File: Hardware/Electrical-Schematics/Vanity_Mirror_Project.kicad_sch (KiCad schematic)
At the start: 38 parts, among them J1 USB_C_Receptacle_USB2.0_14P, SW1 RST, U1 CH340C, U2 ESP-12F, U3 USBLC6-2SC6, U4 XL1509-3.3, U5 SN74AHCT125N, U6 MPR121QR2

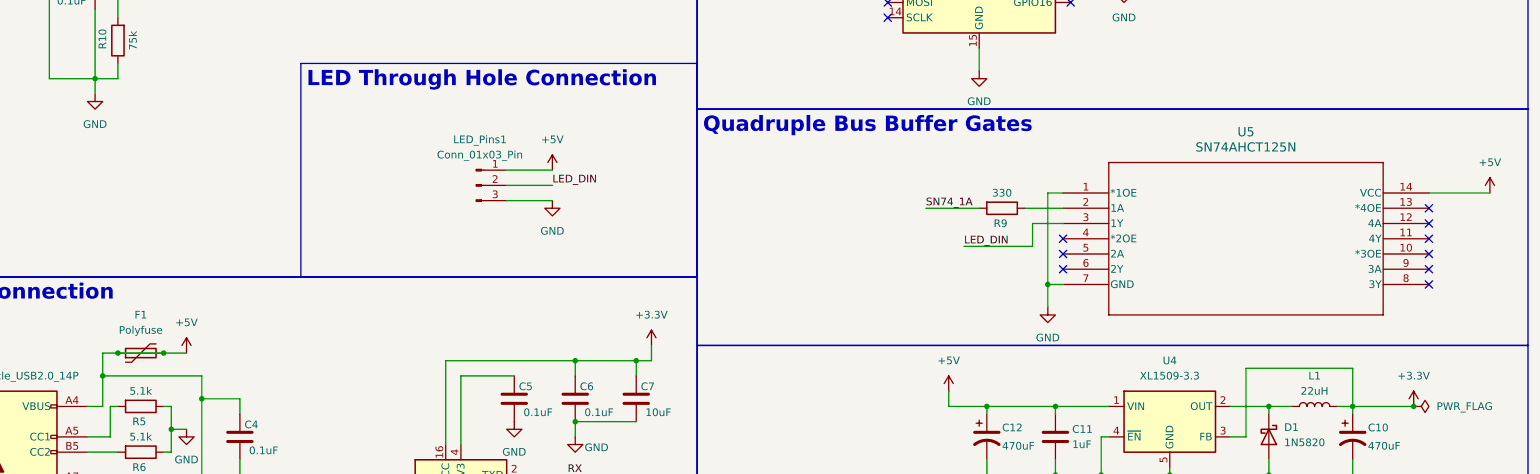
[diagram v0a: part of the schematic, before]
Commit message: PCB Design Progress
Made progress with the PCB design and reorganized the gitignores so that it works.
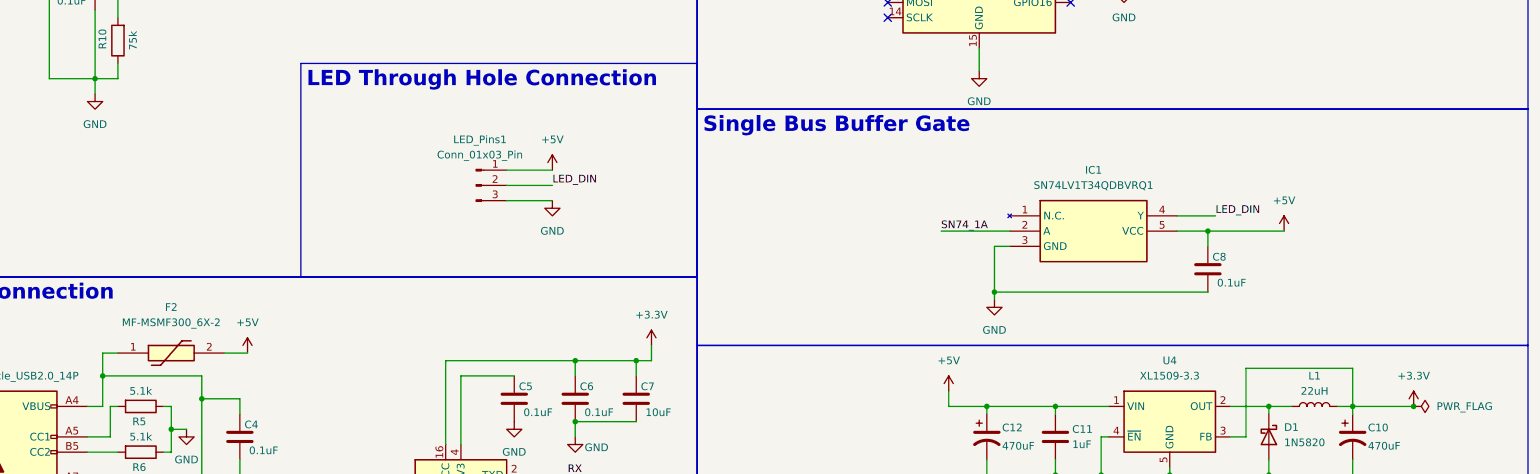
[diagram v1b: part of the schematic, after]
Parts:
- removed F1: Polyfuse, Fuse:Fuse_1206_3216Metric, symbol Device:Polyfuse
- removed R9: 330, Resistor_SMD:R_0603_1608Metric, symbol Device:R
- removed U5: SN74AHCT125N, VanityMirror_FootPrints:SN74AHCT125N, symbol New_Library:SN74AHCT125N
- added C8: 0.1uF, Capacitor_SMD:C_0603_1608Metric, symbol Device:C
- added F2: MF-MSMF300_6X-2, VanityMirror_FootPrints:MFMSMF3006X2, symbol New_Library:MF-MSMF300_6X-2
- added IC1: SN74LV1T34QDBVRQ1, VanityMirror_FootPrints:SOT95P280X145-5N, symbol New_Library:SN74LV1T34QDBVRQ1
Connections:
- net +5V: now also C8.1, F2.2, IC1.5 (VCC); no longer C4.1, J1.A4 (VBUS), J1.A9 (VBUS), J1.B4 (VBUS), J1.B9 (VBUS), U3.5 (VBUS)
- net GND: now also C8.2, IC1.3 (GND)
- net LED_DIN: now also IC1.4 (Y)
- net SN74_1A: now also IC1.2 (A)
- new net: C4.1, F2.1, J1.A4 (VBUS), J1.A9 (VBUS), J1.B4 (VBUS), J1.B9 (VBUS), U3.5 (VBUS)
- no-connect marks 32 -> 23

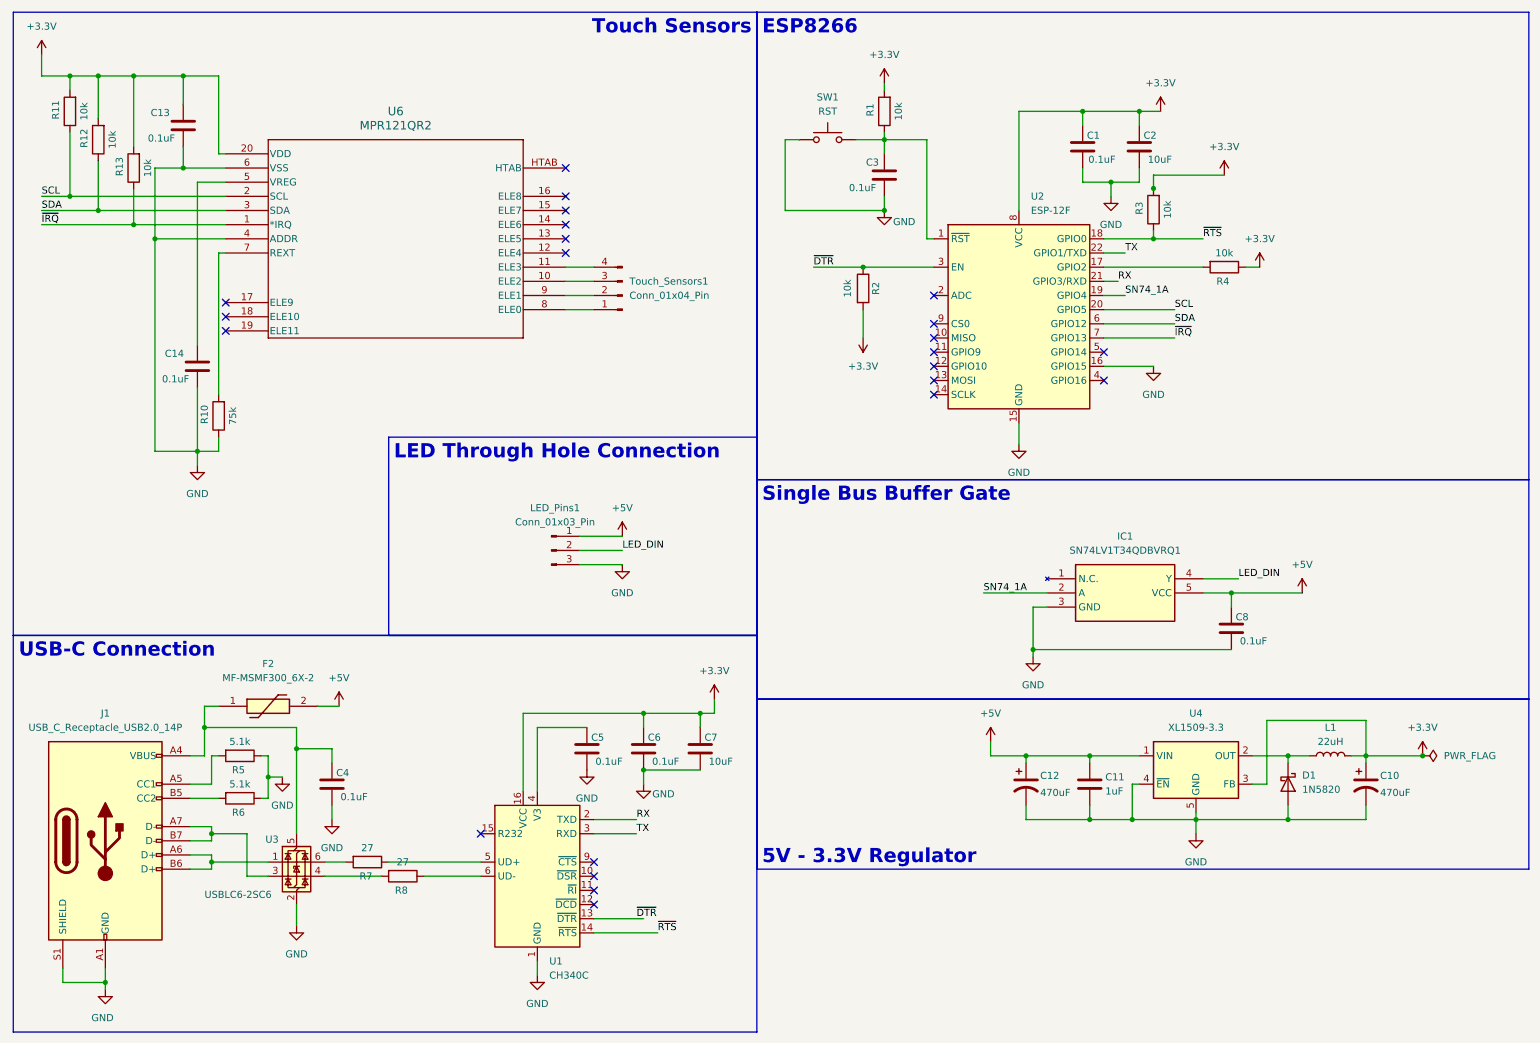
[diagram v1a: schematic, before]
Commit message: Initial PCB layout and Schematic Revisions
Revised some wiring in the schematic and fixed some wiring mistakes. Created an initial layout for the PCB
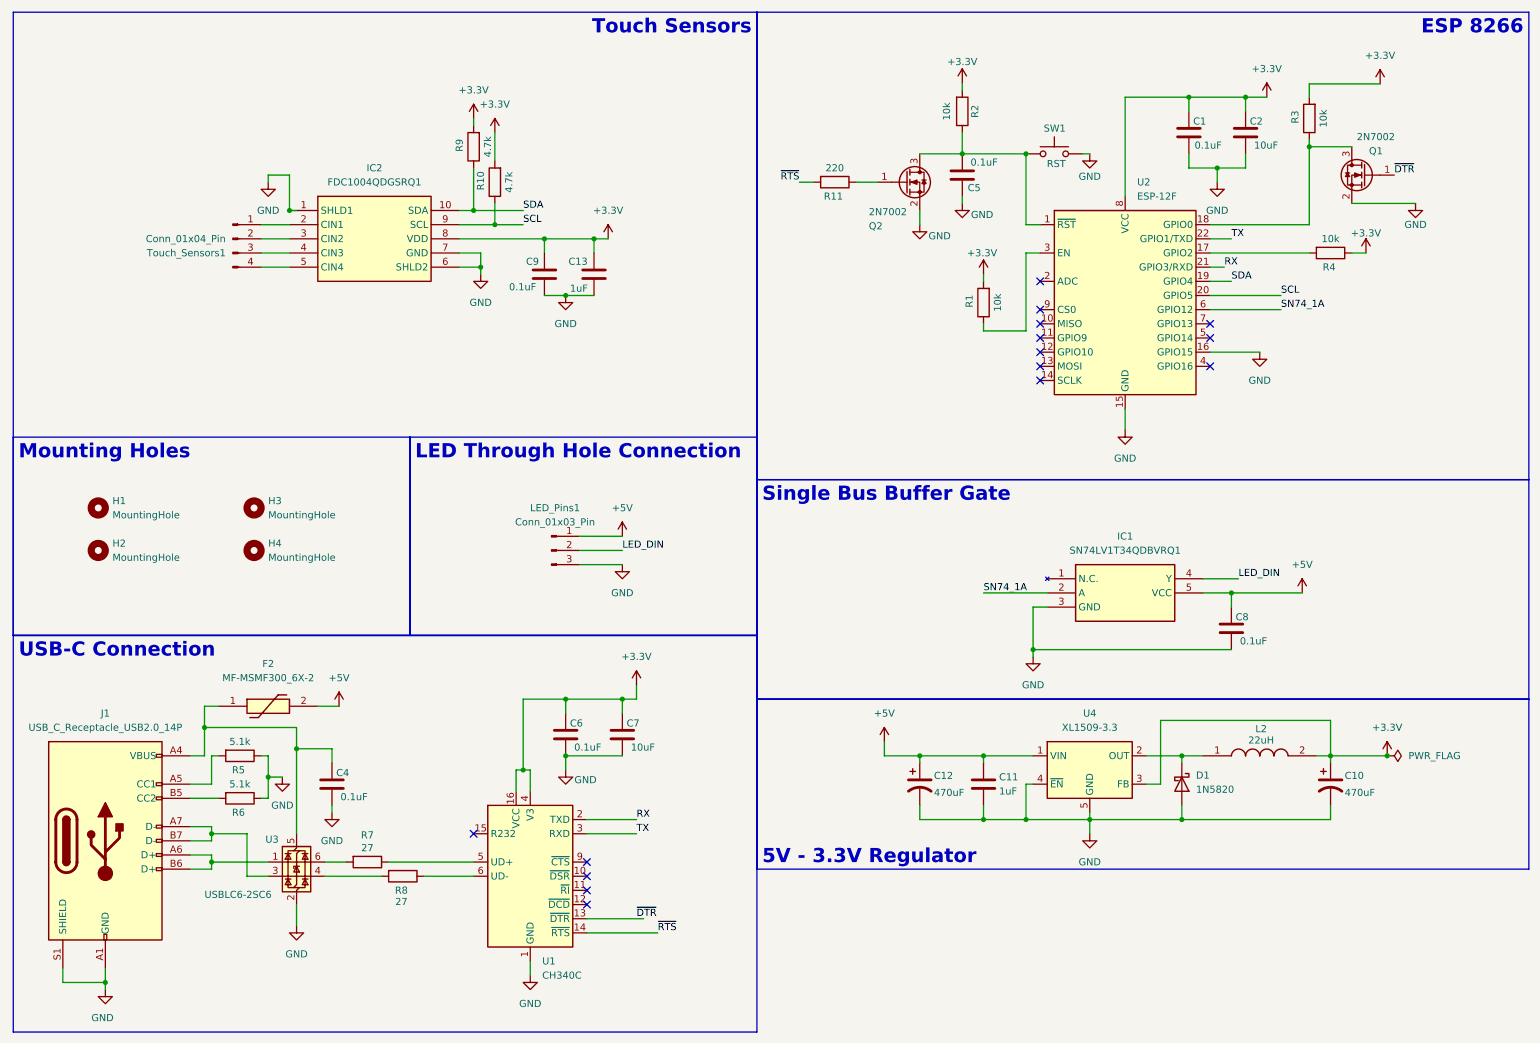
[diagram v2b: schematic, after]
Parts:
- removed C14, C3: 0.1uF, Capacitor_SMD:C_0603_1608Metric, symbol Device:C
- removed L1: 22uH, Inductor_SMD:L_Bourns_SRP1038C_10.0x10.0mm, symbol Device:L
- removed R12, R13: 10k, Resistor_SMD:R_0603_1608Metric, symbol Device:R
- removed U6: MPR121QR2, VanityMirror_FootPrints:QFN20_FRE, symbol New_Library:MPR121QR2
- added C9: 0.1uF, Capacitor_SMD:C_0603_1608Metric, symbol Device:C
- added H1, H2, H3, H4: MountingHole, MountingHole:MountingHole_3.2mm_M3, symbol Mechanical:MountingHole
- added IC2: FDC1004QDGSRQ1, SOP50P490X110-10N, symbol New_Library:FDC1004QDGSRQ1
- added L2: 22uH, INDPM110100X400N, symbol New_Library:SRP1038CC-220M
- added Q1, Q2: 2N7002, Package_TO_SOT_SMD:SOT-23, symbol Transistor_FET:2N7002
- added R9: 4.7k, Resistor_SMD:R_0603_1608Metric, symbol Device:R
- C13: value 0.1uF -> 1uF
- R10: value 75k -> 4.7k
- R11: value 10k -> 220
- SW1: footprint Button_Switch_THT:SW_PUSH_6mm -> Button_Switch_THT:SW_PUSH_1P1T_6x3.5mm_H4.3_APEM_MJTP1243
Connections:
- net +3.3V: now also R10.2, U1.4 (V3), C9.1, IC2.8 (VDD), L2.2, R9.2; no longer R11.2
- net GND: now also C5.1, C9.2, IC2.1 (SHLD1), IC2.6 (SHLD2), IC2.7 (GND), Q1.2 (S), Q2.2 (S); no longer C5.2, R10.1
- net SCL: now also R10.1, IC2.9 (SCL); no longer R11.1
- net SDA: now also U2.19 (GPIO4), IC2.10 (SDA), R9.1; no longer U2.6 (GPIO12)
- net SN74_1A: now also U2.6 (GPIO12); no longer U2.19 (GPIO4)
- net ~{DTR}: now also Q1.1 (G); no longer R2.1, U2.3 (EN)
- net ~{RTS}: now also R11.2; no longer R3.1, U2.18 (GPIO0)
- net at D1.1 (K), U4.2 (OUT): now also L2.1
- net at SW1.2, U2.1 (~{RST}): now also C5.2, R2.1, Q2.3 (D); no longer R1.1
- net at Touch_Sensors1.3 (Pin_3): now also IC2.4 (CIN3)
- net at Touch_Sensors1.4 (Pin_4): now also IC2.5 (CIN4)
- net at Touch_Sensors1.1 (Pin_1): now also IC2.2 (CIN1)
- net at Touch_Sensors1.2 (Pin_2): now also IC2.3 (CIN2)
- net ~{IRQ}: no longer names the net of U2.7 (GPIO13)
- new net: Q1.3 (D), R3.1, U2.18 (GPIO0)
- new net: Q2.1 (G), R11.1
- new net: R1.1, U2.3 (EN)
- no-connect marks 23 -> 15
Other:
- moved on the sheet: C1, C10, C11, C12, C2, C6, C7, D1, R1, R2, R3, R4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

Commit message: 1st PCB design
Finished the routing of the PCB and added BJTs for auto programming and auto resetting.
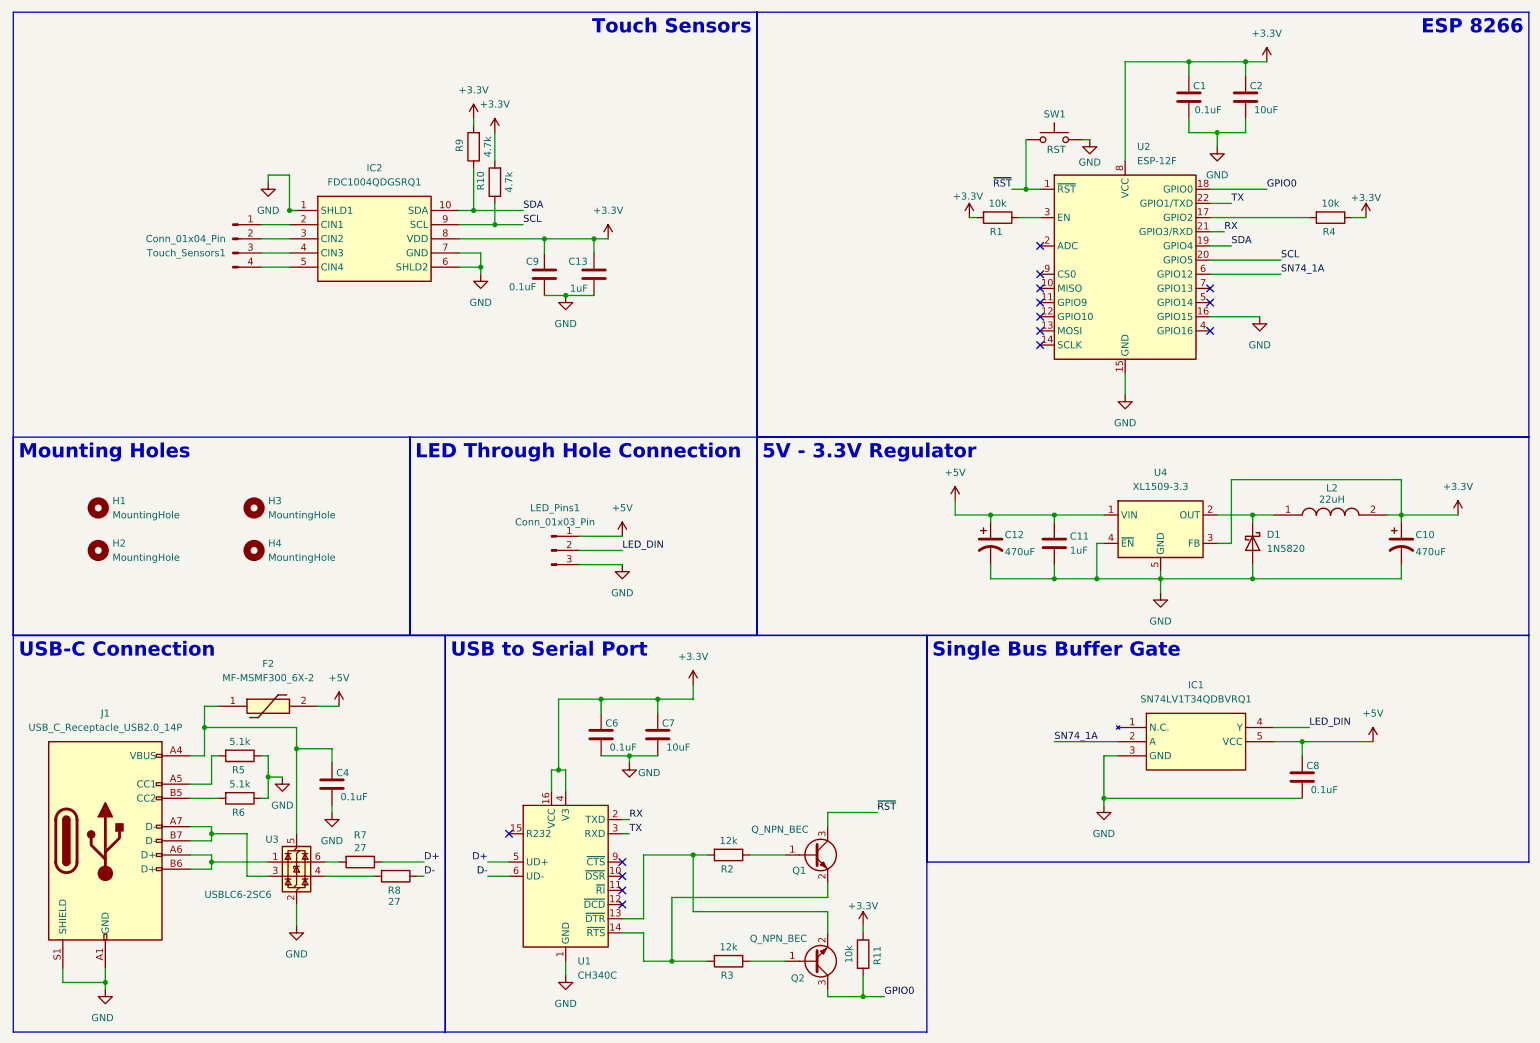
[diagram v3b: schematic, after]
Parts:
- removed C5: 0.1uF, Capacitor_SMD:C_0603_1608Metric, symbol Device:C
- removed Q1, Q2: 2N7002, Package_TO_SOT_SMD:SOT-23, symbol Transistor_FET:2N7002
- added Q1, Q2: Q_NPN_BEC, VanityMirror_FootPrints:PMEG2020EPASX, symbol Transistor_BJT:Q_NPN_BEC
- R11: value 220 -> 10k
- R2, R3: value 10k -> 12k
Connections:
- net +3.3V: now also R11.1; no longer R2.2, R3.2
- net at R3.1: now also Q2.1 (B); no longer U2.18 (GPIO0)
- net ~{RST}: now reaches SW1.2, U2.1 (~{RST})
- net ~{RST}: now also Q1.3 (C); no longer R2.1
- net D+: now reaches R7.1, U1.5 (UD+)
- net D-: now reaches R8.1, U1.6 (UD-)
- net ~{DTR}: no longer names the net of U1.13 (~{DTR})
- net ~{DTR}: now also R2.2, Q2.2 (E)
- net ~{RTS}: no longer names the net of U1.14 (~{RTS})
- net ~{RTS}: now also R3.2, Q1.2 (E); no longer R11.2
- new net: Q1.1 (B), R2.1
- new net GPIO0: Q2.3 (C), R11.2, U2.18 (GPIO0)
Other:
- moved on the sheet: C1, C10, C11, C12, C2, C6, C7, C8, D1, IC1, L2, R1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
